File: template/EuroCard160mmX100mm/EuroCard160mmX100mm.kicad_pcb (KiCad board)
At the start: 2 copper layers, 160 x 100 mm, 0 parts

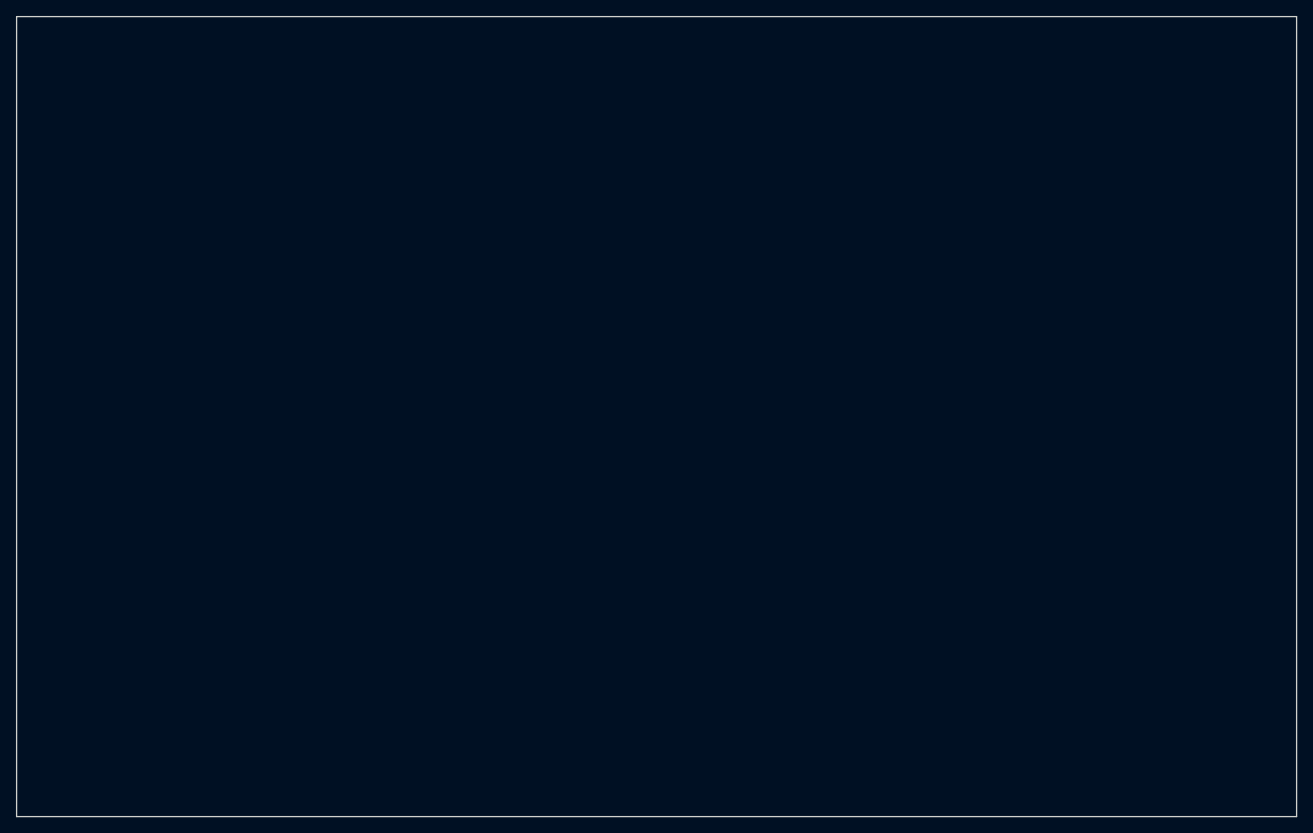
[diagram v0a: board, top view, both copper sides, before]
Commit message: Trimmed edges by .075mm to achieve +0.0/-0.3mm tolerance.
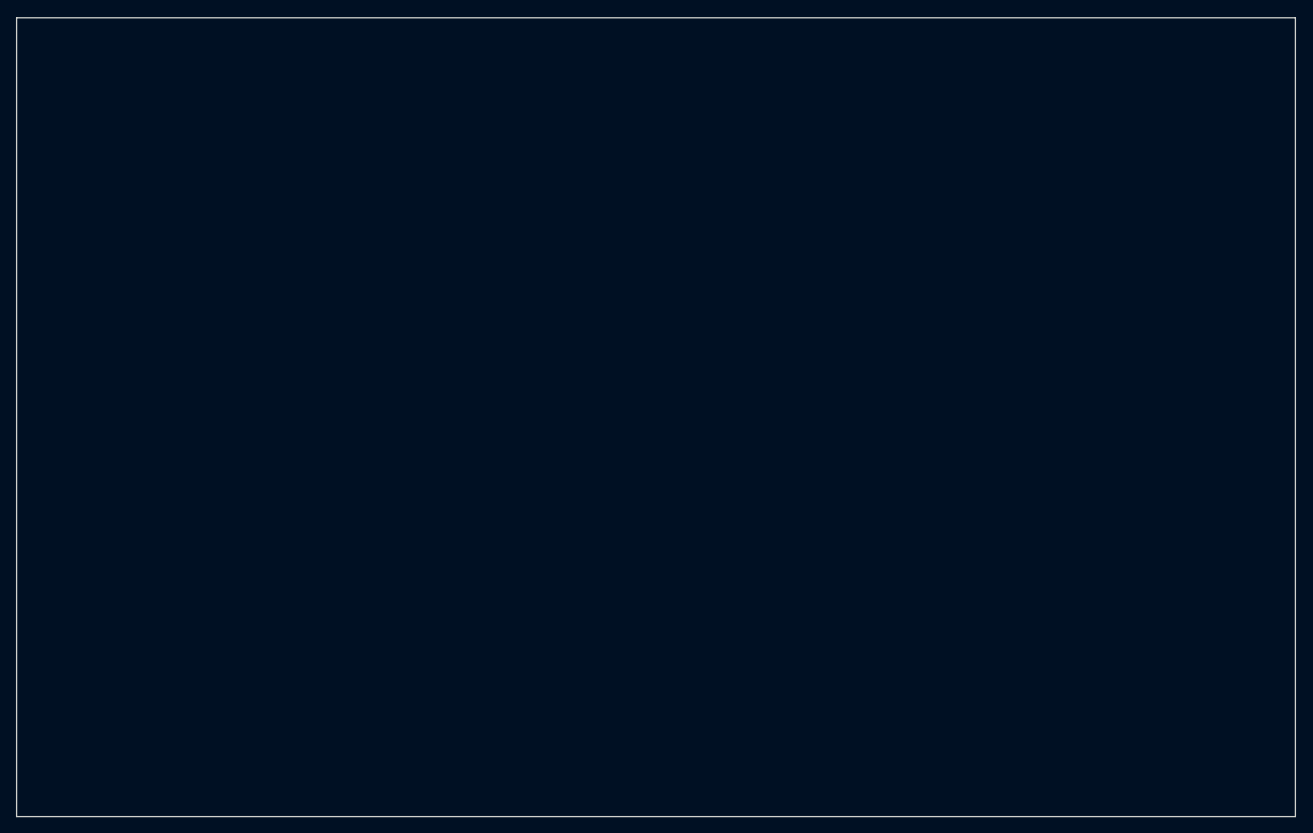
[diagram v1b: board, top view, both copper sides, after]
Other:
- board size 160 x 100 mm -> 159.8 x 99.8 mm
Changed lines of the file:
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@@
     (uvia_drill 0.1)
   )
-  (gr_line (start 55 145) (end 215 145) (angle 90) (layer Edge.Cuts) (width 0.15))
-  (gr_line (start 55 45) (end 55 145) (angle 90) (layer Edge.Cuts) (width 0.15))
-  (gr_line (start 215 45) (end 55 45) (angle 90) (layer Edge.Cuts) (width 0.15))
-  (gr_line (start 215 145) (end 215 45) (angle 90) (layer Edge.Cuts) (width 0.15))
+  (gr_line (start 55 145) (end 214.85 145) (angle 90) (layer Edge.Cuts) (width 0.15))
+  (gr_line (start 55 45.15) (end 55 145) (angle 90) (layer Edge.Cuts) (width 0.15))
+  (gr_line (start 214.84 45.15) (end 55 45.15) (angle 90) (layer Edge.Cuts) (width 0.15))
+  (gr_line (start 214.85 145) (end 214.85 45.15) (angle 90) (layer Edge.Cuts) (width 0.15))
 )
